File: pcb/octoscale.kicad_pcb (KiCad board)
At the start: 2 copper layers, 60 x 96.5 mm, 113 parts, among them J1 USB_C_Receptacle_USB2.0 TYPE-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, J2 Conn_01x04_Male, J3 Molex picoblade vertical C122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, J4 JST-SH, stemma, J5 JST-SH, J6 JST-SH, J7 Conn_01x04_Male, Q1 AO3415_C181094, Q2 MMBT44032T, Q3 S8050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

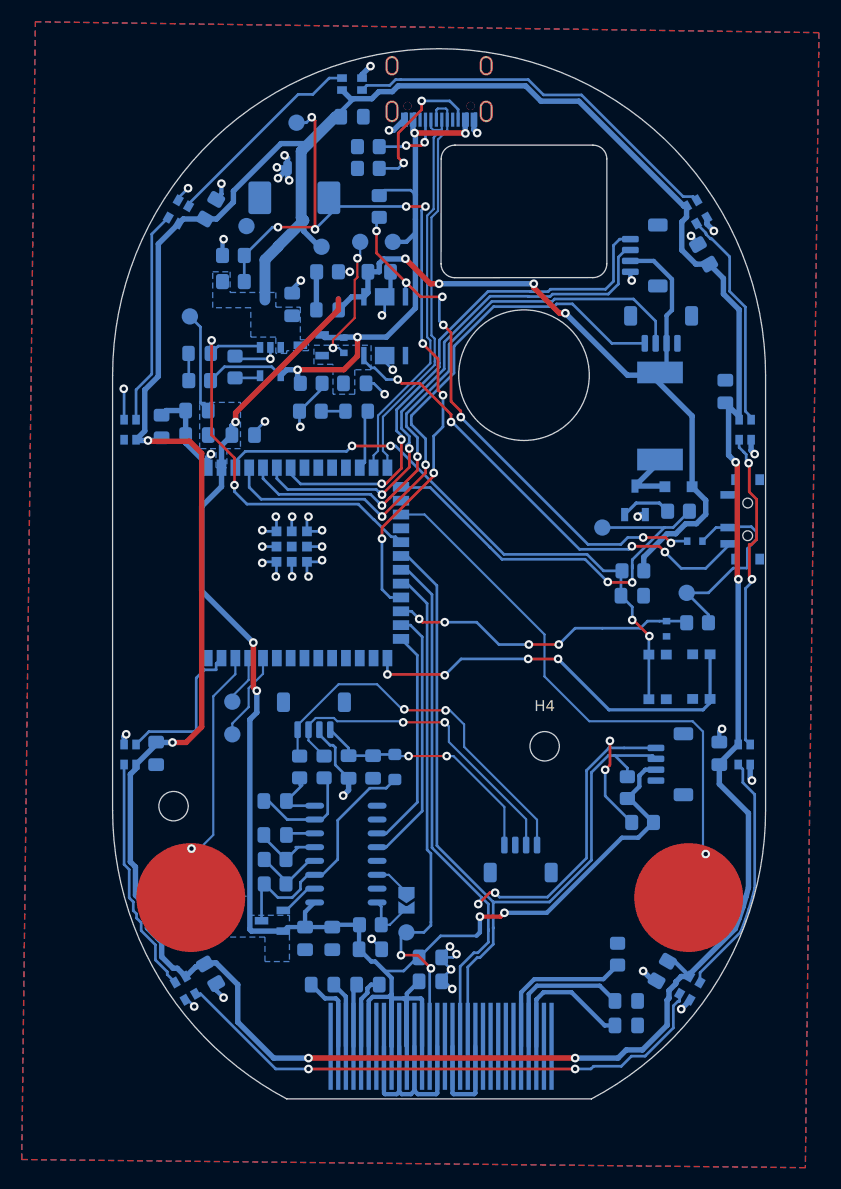
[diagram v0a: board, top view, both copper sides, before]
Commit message: Tweak to layout and power ldo en
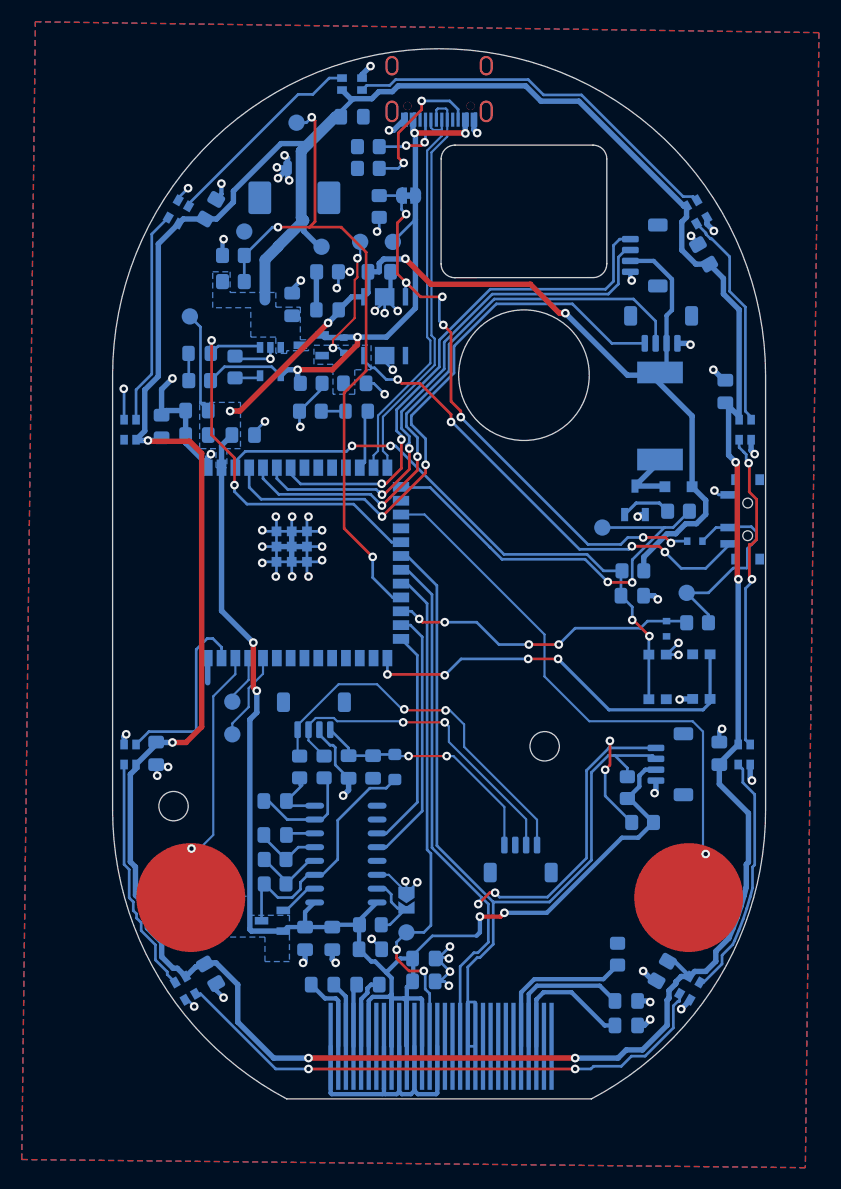
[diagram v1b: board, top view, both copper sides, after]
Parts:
- added JP2: SolderJumper_2_Bridged, Jumper:SolderJumper-2_P1.3mm_Bridged_RoundedPad1.0x1.5mm, B.Cu at (167.2, 58.5)
- moved C29 0.61 mm to (168.6, 128.6)
- moved C28 0.60 mm to (168.6, 130.7)
- moved TP10 0.54 mm to (152.1, 61.8)
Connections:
- R15 pad 1: VBUS -> LDO_EN
- R15 pad 2: LDO_EN -> GND
- U4 pad 15: (no net) -> Net-(JP1-Pad2)
- U4 pad 16: Net-(JP1-Pad2) -> +3V3
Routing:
- net GND: track 128.6 -> 186.0 mm, vias 50 -> 71
- net BATT_SENSE: track 73.4 -> 62.8 mm, vias 9 -> 3
- net SDA: track 88.7 -> 83.3 mm
- net VBUS: track 58.7 -> 53.7 mm
- net LDO_EN: track 50.6 -> 54.3 mm
- net TOUCH_2: track 53.2 -> 49.6 mm
- net NEOPIXELS: track 14.3 -> 17.5 mm
- net Net-(JP1-Pad2): track 5.15 -> 6.80 mm
- net +3V3: track 248.3 -> 247.2 mm, vias 9 -> 8
- net SCL: track 86.6 -> 85.9 mm
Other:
- board text added: "cut to disable wake on usb"

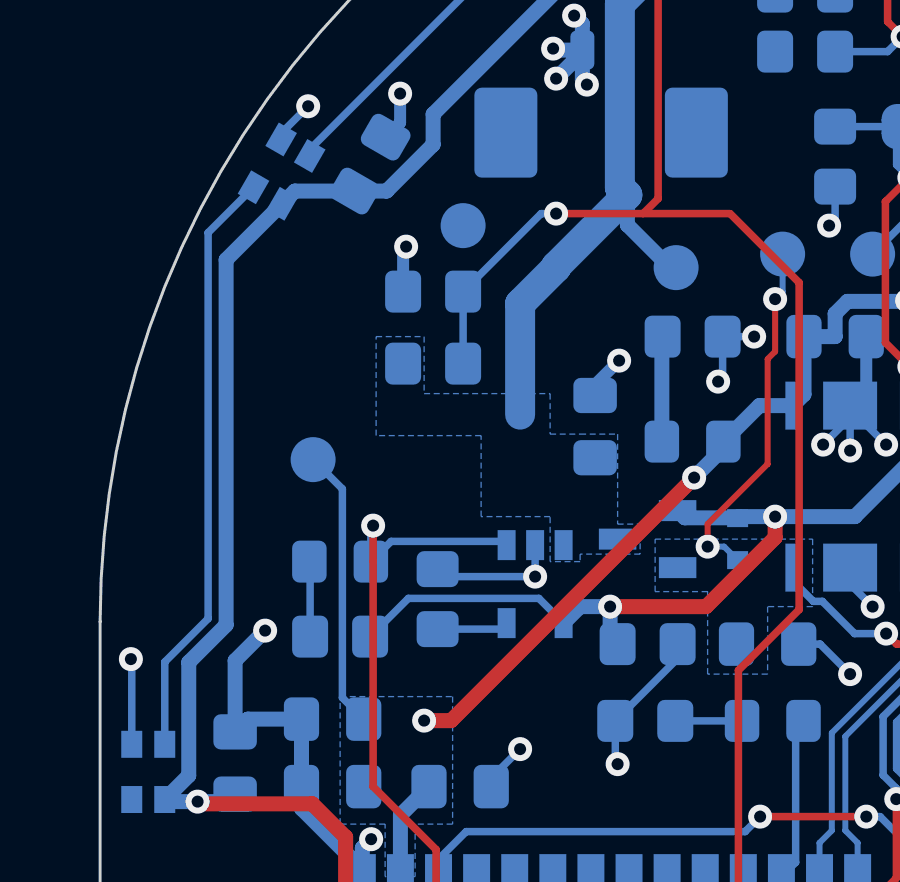
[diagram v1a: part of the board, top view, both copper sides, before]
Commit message: Tweak charging speed
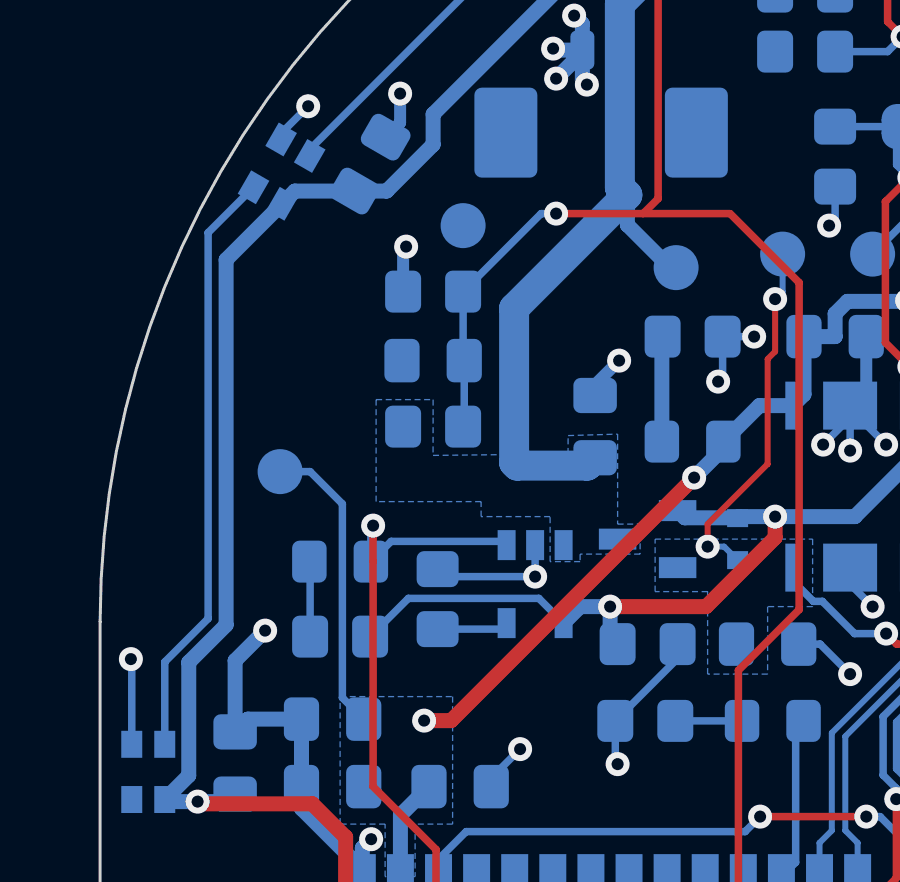
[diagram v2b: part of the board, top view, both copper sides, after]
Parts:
- added C30: 100nF, Capacitor_SMD:C_0805_2012Metric_Pad1.18x1.45mm_HandSolder, B.Cu at (151.1, 66.3)
- moved R16 2.10 mm to (151.1, 68.5)
- moved TP12 1.17 mm to (146.0, 70.0)
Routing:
- net +BATT: track 304.1 -> 308.7 mm
- net BATT_SENSE: track 62.8 -> 65.1 mm
- net +3V3: track 247.2 -> 247.8 mm

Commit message: Move Batt sense to adc capable pin
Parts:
- R5: value 2K -> 3.3K
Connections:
- U5 pad 10: unconnected-(U5-Pad10) -> BATT_SENSE
- U5 pad 23: BATT_SENSE -> unconnected-(U5-Pad23)
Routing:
- net BATT_SENSE: track 65.1 -> 51.0 mm

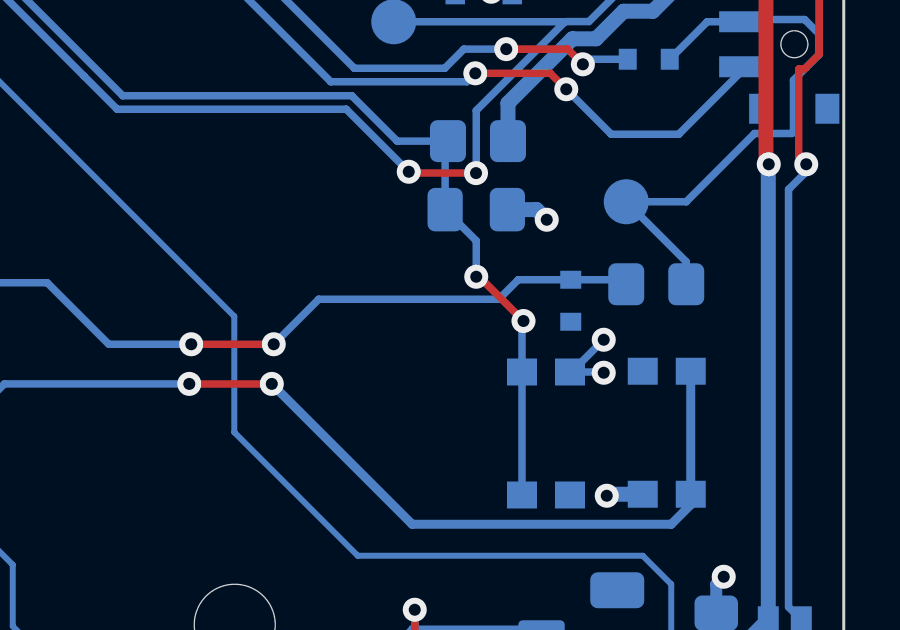
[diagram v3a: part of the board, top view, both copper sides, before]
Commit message: Change zener footprint
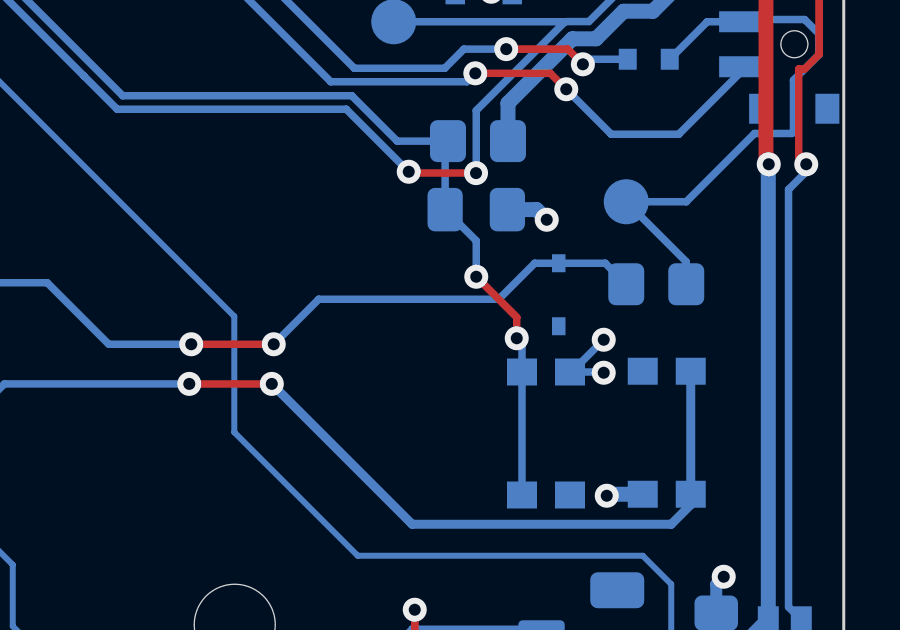
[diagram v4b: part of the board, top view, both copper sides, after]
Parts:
- D16: footprint Diode_SMD:D_SOD-523 -> Diode_SMD:D_SOD-323
- moved D16 0.45 mm to (190.5, 98.1)
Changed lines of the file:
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@@
     )
   )
-  (footprint "Diode_SMD:D_SOD-523" (layer "B.Cu")
-    (at 190.9 98.3 -90)
-    (descr "http://www.diodes.com/datasheets/ap02001.pdf p.144")
-    (tags "Diode SOD523")
+  (footprint "Diode_SMD:D_SOD-323" (layer "B.Cu")
+    (at 190.5 98.1 -90)
+    (descr "SOD-323")
+    (tags "SOD-323")
     (property "Sheetfile" "octoscale.kicad_sch")
     (property "Sheetname" "")
     (attr smd)
-    (fp_text reference "D16" (at 0 1.3 90) (layer "B.SilkS")
-      (effects (font (size 1 1) (thickness 0.15)) (justify mirror))
-    )
-    (fp_text value "3v Zener, BZT52C3V0T" (at 0 -1.4 90) (layer "B.Fab")
-      (effects (font (size 1 1) (thickness 0.15)) (justify mirror))
-    )
-    (fp_text user "${REFERENCE}" (at 0 1.3 90) (layer "B.Fab")
-      (effects (font (size 1 1) (thickness 0.15)) (justify mirror))
-    )
-    (fp_line (start 0.7 0.6) (end -1.15 0.6) (layer "B.SilkS") (width 0.12))
-    (fp_line (start 0.7 -0.6) (end -1.15 -0.6) (layer "B.SilkS") (width 0.12))
-    (fp_line (start -1.15 0.6) (end -1.15 -0.6) (layer "B.SilkS") (width 0.12))
-    (fp_line (start -1.25 0.7) (end 1.25 0.7) (layer "B.CrtYd") (width 0.05))
-    (fp_line (start 1.25 0.7) (end 1.25 -0.7) (layer "B.CrtYd") (width 0.05))
-    (fp_line (start -1.25 -0.7) (end -1.25 0.7) (layer "B.CrtYd") (width 0.05))
-    (fp_line (start 1.25 -0.7) (end -1.25 -0.7) (layer "B.CrtYd") (width 0.05))
-    (fp_line (start 0.1 0.2) (end -0.2 0) (layer "B.Fab") (width 0.1))
-    (fp_line (start 0.1 -0.2) (end 0.1 0.2) (layer "B.Fab") (width 0.1))
-    (fp_line (start -0.2 -0.2) (end -0.2 0.2) (layer "B.Fab") (width 0.1))
-    (fp_line (start 0.65 0.45) (end 0.65 -0.45) (layer "B.Fab") (width 0.1))
-    (fp_line (start -0.65 -0.45) (end -0.65 0.45) (layer "B.Fab") (width 0.1))
-    (fp_line (start -0.65 0.45) (end 0.65 0.45) (layer "B.Fab") (width 0.1))
-    (fp_line (start -0.2 0) (end -0.35 0) (layer "B.Fab") (width 0.1))
-    (fp_line (start 0.65 -0.45) (end -0.65 -0.45) (layer "B.Fab") (width 0.1))
-    (fp_line (start 0.1 0) (end 0.25 0) (layer "B.Fab") (width 0.1))
-    (fp_line (start -0.2 0) (end 0.1 -0.2) (layer "B.Fab") (width 0.1))
-    (pad "1" smd rect (at -0.7 0 90) (size 0.6 0.7) (layers "B.Cu" "B.Paste" "B.Mask")
+    (fp_text reference "D16" (at -0.25 1.55 90) (layer "B.SilkS")
+      (effects (font (size 1 1) (thickness 0.15)) (justify mirror))
+    )
+    (fp_text value "3v Zener, BZT52C3V0T" (at 0.1 -1.9 90) (layer "B.Fab")
+      (effects (font (size 1 1) (thickness 0.15)) (justify mirror))
+    )
+    (fp_text user "${REFERENCE}" (at 0 1.85 90) (layer "B.Fab")
+      (effects (font (size 1 1) (thickness 0.15)) (justify mirror))
+    )
+    (fp_line (start -1.5 0.85) (end 1.05 0.85) (layer "B.SilkS") (width 0.12))
+    (fp_line (start -1.5 0.85) (end -1.5 -0.85) (layer "B.SilkS") (width 0.12))
+    (fp_line (start -1.5 -0.85) (end 1.05 -0.85) (layer "B.SilkS") (width 0.12))
+    (fp_line (start -1.6 -0.95) (end 1.6 -0.95) (layer "B.CrtYd") (width 0.05))
+    (fp_line (start -1.6 0.95) (end -1.6 -0.95) (layer "B.CrtYd") (width 0.05))
+    (fp_line (start 1.6 0.95) (end 1.6 -0.95) (layer "B.CrtYd") (width 0.05))
+    (fp_line (start -1.6 0.95) (end 1.6 0.95) (layer "B.CrtYd") (width 0.05))
+    (fp_line (start 0.2 0.35) (end 0.2 -0.35) (layer "B.Fab") (width 0.1))
+    (fp_line (start -0.9 0.7) (end 0.9 0.7) (layer "B.Fab") (width 0.1))
+    (fp_line (start 0.2 -0.35) (end -0.3 0) (layer "B.Fab") (width 0.1))
+    (fp_line (start -0.9 -0.7) (end -0.9 0.7) (layer "B.Fab") (width 0.1))
+    (fp_line (start 0.9 0.7) (end 0.9 -0.7) (layer "B.Fab") (width 0.1))
+    (fp_line (start 0.9 -0.7) (end -0.9 -0.7) (layer "B.Fab") (width 0.1))
+    (fp_line (start -0.3 0) (end -0.5 0) (layer "B.Fab") (width 0.1))
+    (fp_line (start 0.2 0) (end 0.45 0) (layer "B.Fab") (width 0.1))
+    (fp_line (start -0.3 0) (end 0.2 0.35) (layer "B.Fab") (width 0.1))
+    (fp_line (start -0.3 0.35) (end -0.3 -0.35) (layer "B.Fab") (width 0.1))
+    (pad "1" smd rect (at -1.05 0 270) (size 0.6 0.45) (layers "B.Cu" "B.Paste" "B.Mask")
       (net 81 "POWER_SWITCH_SENSE") (pinfunction "K") (pintype "passive"))
-    (pad "2" smd rect (at 0.7 0 90) (size 0.6 0.7) (layers "B.Cu" "B.Paste" "B.Mask")
+    (pad "2" smd rect (at 1.05 0 270) (size 0.6 0.45) (layers "B.Cu" "B.Paste" "B.Mask")
       (net 3 "GND") (pinfunction "A") (pintype "passive"))
-    (model "${KICAD6_3DMODEL_DIR}/Diode_SMD.3dshapes/D_SOD-523.wrl"
+    (model "${KICAD6_3DMODEL_DIR}/Diode_SMD.3dshapes/D_SOD-323.wrl"
       (offset (xyz 0 0 0))
       (scale (xyz 1 1 1))
@@
   (segment (start 168 100.735) (end 166.5 99.235) (width 0.25) (layer "B.Cu") (net 46))
   (segment (start 168 114.25) (end 168 100.735) (width 0.25) (layer "B.Cu") (net 46))
-  (segment (start 189.325 98.975) (end 187.85 97.5) (width 0.25) (layer "F.Cu") (net 49))
   (segment (start 162 81.5) (end 165.5395 81.5) (width 0.25) (layer "F.Cu") (net 49))
-  (segment (start 187.85 97.5) (end 187.75 97.5) (width 0.25) (layer "F.Cu") (net 49))
+  (segment (start 189.1 98.85) (end 187.75 97.5) (width 0.25) (layer "F.Cu") (net 49))
+  (segment (start 189.1 99.55) (end 189.1 98.85) (width 0.25) (layer "F.Cu") (net 49))
   (via (at 162 81.5) (size 0.8) (drill 0.4) (layers "F.Cu" "B.Cu") (net 49))
   (via (at 165.5395 81.5) (size 0.8) (drill 0.4) (layers "F.Cu" "B.Cu") (net 49))
   (via (at 187.75 97.5) (size 0.8) (drill 0.4) (layers "F.Cu" "B.Cu") (net 49))
-  (via (at 189.325 98.975) (size 0.8) (drill 0.4) (layers "F.Cu" "B.Cu") (net 49))
+  (via (at 189.1 99.55) (size 0.8) (drill 0.4) (layers "F.Cu" "B.Cu") (net 49))
   (segment (start 175.966507 91.466507) (end 183.602225 91.466507) (width 0.25) (layer "B.Cu") (net 49))
   (segment (start 186.7125 93.07452) (end 186.808013 92.979007) (width 0.25) (layer "B.Cu") (net 49))
-  (segment (start 189.275 100.675) (end 189.275 99.025) (width 0.25) (layer "B.Cu") (net 49))
   (segment (start 187.75 96.3) (end 187.75 97.4) (width 0.25) (layer "B.Cu") (net 49))
   (segment (start 185.114725 92.979007) (end 186.808013 92.979007) (width 0.25) (layer "B.Cu") (net 49))
   (segment (start 165.5395 81.5) (end 166 81.5) (width 0.25) (layer "B.Cu") (net 49))
   (segment (start 166 81.5) (end 175.966507 91.466507) (width 0.25) (layer "B.Cu") (net 49))
+  (segment (start 189.275 99.725) (end 189.275 100.675) (width 0.25) (layer "B.Cu") (net 49))
   (segment (start 189.275 100.675) (end 189.275 104.775) (width 0.25) (layer "B.Cu") (net 49))
   (segment (start 187.75 97.4) (end 187.7 97.45) (width 0.25) (layer "B.Cu") (net 49))
-  (segment (start 189.275 99.025) (end 189.325 98.975) (width 0.25) (layer "B.Cu") (net 49))
   (segment (start 186.7125 95.2625) (end 186.7125 93.07452) (width 0.25) (layer "B.Cu") (net 49))
   (segment (start 186.7125 95.2625) (end 187.75 96.3) (width 0.25) (layer "B.Cu") (net 49))
@@
   (segment (start 183.602225 91.466507) (end 185.114725 92.979007) (width 0.25) (layer "B.Cu") (net 49))
   (segment (start 152.00048 81.54952) (end 151.28 82.27) (width 0.25) (layer "B.Cu") (net 49))
+  (segment (start 189.1 99.55) (end 189.275 99.725) (width 0.25) (layer "B.Cu") (net 49))
   (segment (start 162 81.5) (end 161.95048 81.54952) (width 0.25) (layer "B.Cu") (net 49))
   (segment (start 147.685 100.205978) (end 147.685 107.571762) (width 0.25) (layer "B.Cu") (net 50))
@@
   (via (at 170.52258 97.7) (size 0.8) (drill 0.4) (layers "F.Cu" "B.Cu") (net 81))
   (via (at 178.25 99.75) (size 0.8) (drill 0.4) (layers "F.Cu" "B.Cu") (net 81))
-  (segment (start 189.15 97.6) (end 188.5 98.25) (width 0.25) (layer "B.Cu") (net 81))
   (segment (start 166.5 96.695) (end 167.46954 96.695) (width 0.25) (layer "B.Cu") (net 81))
+  (segment (start 182.5 98.25) (end 188.5 98.25) (width 0.25) (layer "B.Cu") (net 81))
   (segment (start 173.45 97.7) (end 175.5 99.75) (width 0.25) (layer "B.Cu") (net 81))
   (segment (start 167.46954 96.695) (end 168.17454 97.4) (width 0.25) (layer "B.Cu") (net 81))
-  (segment (start 182.5 98.25) (end 181 99.75) (width 0.25) (layer "B.Cu") (net 81))
+  (segment (start 188.5 98.25) (end 189.7 97.05) (width 0.25) (layer "B.Cu") (net 81))
+  (segment (start 189.7 97.05) (end 192.05 97.05) (width 0.25) (layer "B.Cu") (net 81))
   (segment (start 170.52258 97.7) (end 173.45 97.7) (width 0.25) (layer "B.Cu") (net 81))
-  (segment (start 189.15 97.6) (end 192.6 97.6) (width 0.25) (layer "B.Cu") (net 81))
-  (segment (start 192.75 97.75) (end 192.6 97.6) (width 0.25) (layer "B.Cu") (net 81))
   (segment (start 175.5 99.75) (end 178.25 99.75) (width 0.25) (layer "B.Cu") (net 81))
-  (segment (start 182.5 98.25) (end 188.5 98.25) (width 0.25) (layer "B.Cu") (net 81))
+  (segment (start 192.05 97.05) (end 192.75 97.75) (width 0.25) (layer "B.Cu") (net 81))
+  (segment (start 181 99.75) (end 182.5 98.25) (width 0.25) (layer "B.Cu") (net 81))
   (segment (start 163.3 74.6) (end 163.3 63.7) (width 0.25) (layer "F.Cu") (net 82))
   (segment (start 158.6 51.6) (end 158.6 60.9) (width 0.25) (layer "F.Cu") (net 82))
